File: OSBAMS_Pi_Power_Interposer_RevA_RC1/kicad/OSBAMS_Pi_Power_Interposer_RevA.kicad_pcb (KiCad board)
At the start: 2 copper layers, 57 x 22 mm, 4 parts, among them J1 43045-0400, J2 2x20 stacking socket, K1 KEY M2.5, K2 KEY M2.5

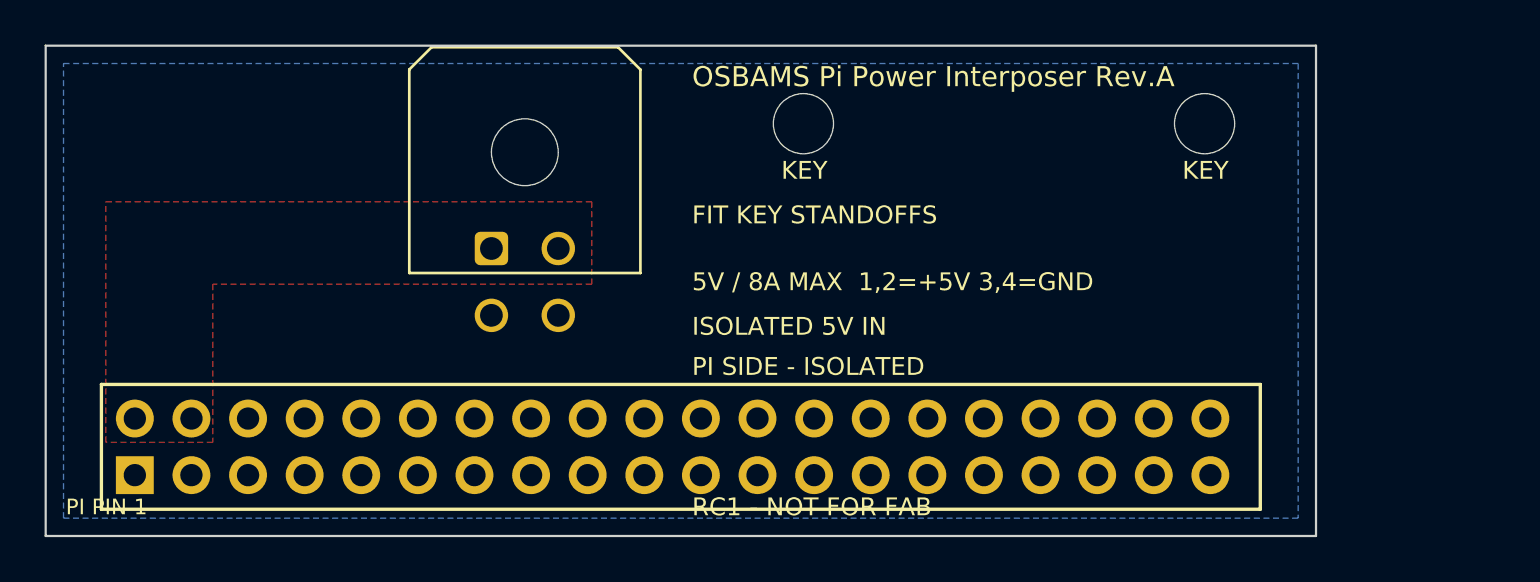
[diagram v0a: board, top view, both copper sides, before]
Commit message: F1 -> Littelfuse 407 8A time-lag (0407008.WR); F2 verified; interposer to HAT+ geometry
Remove 0453008.MRL (very fast-acting). F1 datasheet values and 1206 land pattern
implemented; F2 footprint verified against 451/453 datasheet. Interposer now 65 mm
with M2.5 mounting holes per HAT+ spec. RC2 still gated: socket MPN, Pi 5 STEP
keying check, KiCad 10 ERC.

Co-Authored-By: Claude Sonnet 5.5 <noreply@anthropic.com>
Claude-Session: https://claude.ai/code/session_01ENatZXrEDA18PaxUrZWrpi
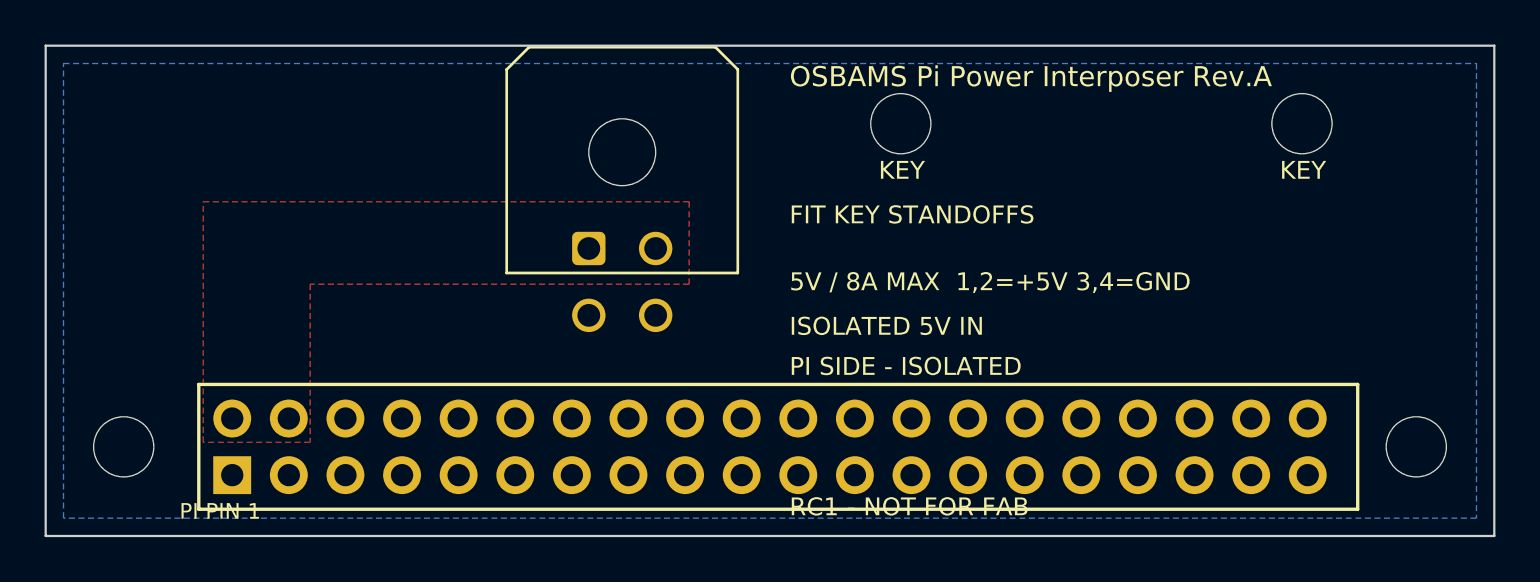
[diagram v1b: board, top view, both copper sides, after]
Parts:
- added M1: M2.5 to Pi, OSBAMS_PiPwr:MountingHole_2.7mm_M2.5, F.Cu at (3.50, 20.0)
- added M2: M2.5 to Pi, OSBAMS_PiPwr:MountingHole_2.7mm_M2.5, F.Cu at (61.5, 20.0)
- moved J1 4.37 mm to (24.4, 11.1)
- moved J2 4.37 mm to (8.37, 20.0)
- moved K1 4.37 mm to (38.4, 5.50)
- moved K2 4.37 mm to (56.4, 5.50)
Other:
- board size 57 x 22 mm -> 65 x 22 mm

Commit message: Pi 5 drawing-based 180-degree key check; move key posts onto bare PCB
Official drawing RP-008347 digitised: reversed posts now land on bare PCB (1.6/3.3 mm clear
of components); correct orientation hangs beyond the Pi edge. Gate: key check passes in plan
view; heights pending SSW-120 drawing.

Co-Authored-By: Claude Sonnet 5.5 <noreply@anthropic.com>
Claude-Session: https://claude.ai/code/session_01ENatZXrEDA18PaxUrZWrpi
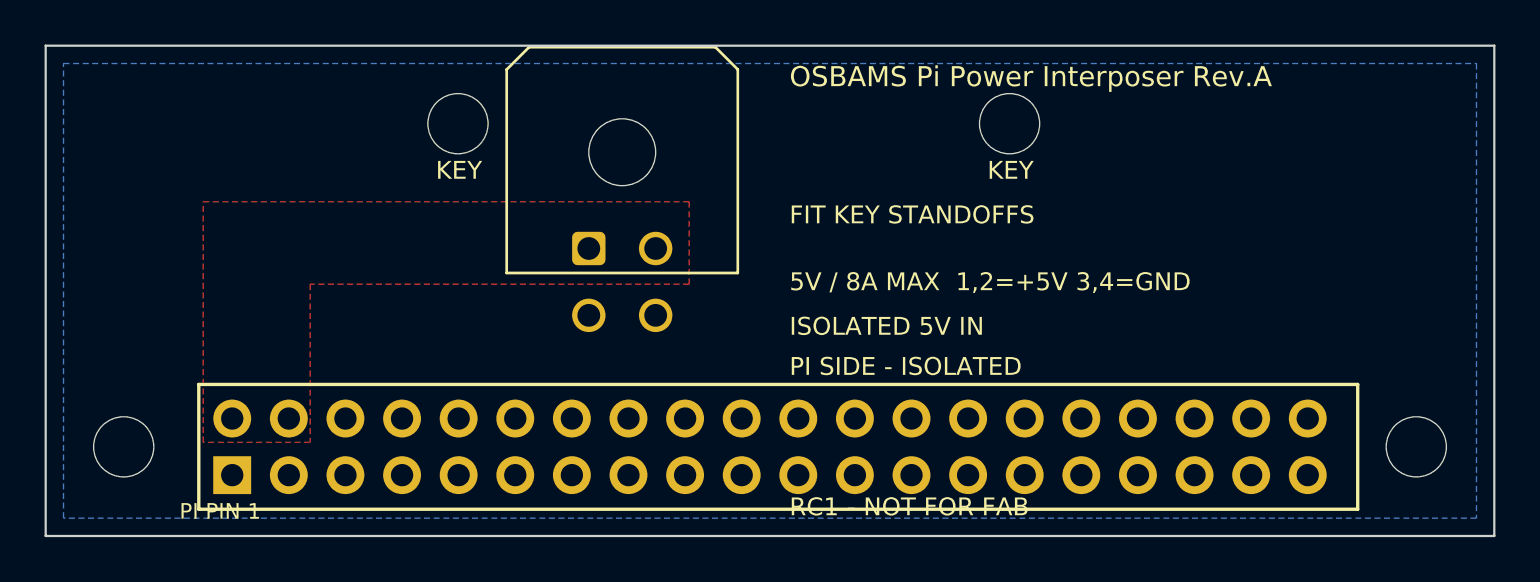
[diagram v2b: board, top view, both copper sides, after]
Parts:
- moved K1 19.9 mm to (18.5, 5.50)
- moved K2 13.1 mm to (43.2, 5.50)
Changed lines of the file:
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@@
   (net 1 "5V_PI")
   (net 2 "PI_GND")
+  (footprint "OSBAMS_PiPwr:KeyStandoff_M2.5" (layer "F.Cu")
+    (at 18.5 5.5)
+    (fp_text reference "K1" (at 0 0) (layer "F.Fab")
+        (effects (font (size 1.27 1.27) (thickness 0.15)))
+    )
+    (fp_text value "KEY M2.5" (at 0 0) (layer "F.SilkS") hide
+        (effects (font (size 1.27 1.27) (thickness 0.15)))
+    )
+    (pad "" np_thru_hole circle (at 0 0) (size 2.7 2.7) (drill 2.7) (layers "F&B.Cu" "*.Mask"))
+  )
+  (footprint "OSBAMS_PiPwr:KeyStandoff_M2.5" (layer "F.Cu")
+    (at 43.25 5.5)
+    (fp_text reference "K2" (at 0 0) (layer "F.Fab")
+        (effects (font (size 1.27 1.27) (thickness 0.15)))
+    )
+    (fp_text value "KEY M2.5" (at 0 0) (layer "F.SilkS") hide
+        (effects (font (size 1.27 1.27) (thickness 0.15)))
+    )
+    (pad "" np_thru_hole circle (at 0 0) (size 2.7 2.7) (drill 2.7) (layers "F&B.Cu" "*.Mask"))
+  )
   (footprint "OSBAMS_PiPwr:MountingHole_2.7mm_M2.5" (layer "F.Cu")
     (at 61.5 20)
     (fp_text reference "M2" (at 0 0) (layer "F.Fab")
-        (effects (font (size 1.27 1.27) (thickness 0.15)))
-    )
-    (fp_text value "M2.5 to Pi" (at 0 0) (layer "F.SilkS") hide
-        (effects (font (size 1.27 1.27) (thickness 0.15)))
-    )
-    (pad "" np_thru_hole circle (at 0 0) (size 2.7 2.7) (drill 2.7) (layers "F&B.Cu" "*.Mask"))
-  )
-  (footprint "OSBAMS_PiPwr:KeyStandoff_M2.5" (layer "F.Cu")
-    (at 38.37 5.5)
-    (fp_text reference "K1" (at 0 0) (layer "F.Fab")
-        (effects (font (size 1.27 1.27) (thickness 0.15)))
-    )
-    (fp_text value "KEY M2.5" (at 0 0) (layer "F.SilkS") hide
-        (effects (font (size 1.27 1.27) (thickness 0.15)))
-    )
-    (pad "" np_thru_hole circle (at 0 0) (size 2.7 2.7) (drill 2.7) (layers "F&B.Cu" "*.Mask"))
-  )
-  (footprint "OSBAMS_PiPwr:KeyStandoff_M2.5" (layer "F.Cu")
-    (at 56.37 5.5)
-    (fp_text reference "K2" (at 0 0) (layer "F.Fab")
-        (effects (font (size 1.27 1.27) (thickness 0.15)))
-    )
-    (fp_text value "KEY M2.5" (at 0 0) (layer "F.SilkS") hide
-        (effects (font (size 1.27 1.27) (thickness 0.15)))
-    )
-    (pad "" np_thru_hole circle (at 0 0) (size 2.7 2.7) (drill 2.7) (layers "F&B.Cu" "*.Mask"))
-  )
-  (footprint "OSBAMS_PiPwr:MountingHole_2.7mm_M2.5" (layer "F.Cu")
-    (at 3.5 20)
-    (fp_text reference "M1" (at 0 0) (layer "F.Fab")
         (effects (font (size 1.27 1.27) (thickness 0.15)))
     )
@@
     )
   )
+  (footprint "OSBAMS_PiPwr:MountingHole_2.7mm_M2.5" (layer "F.Cu")
+    (at 3.5 20)
+    (fp_text reference "M1" (at 0 0) (layer "F.Fab")
+        (effects (font (size 1.27 1.27) (thickness 0.15)))
+    )
+    (fp_text value "M2.5 to Pi" (at 0 0) (layer "F.SilkS") hide
+        (effects (font (size 1.27 1.27) (thickness 0.15)))
+    )
+    (pad "" np_thru_hole circle (at 0 0) (size 2.7 2.7) (drill 2.7) (layers "F&B.Cu" "*.Mask"))
+  )
   (gr_line (start 65 2) (end 65 24)
     (stroke (width 0.1) (type default)) (layer "Edge.Cuts"))
+  (gr_line (start 0 24) (end 0 2)
+    (stroke (width 0.1) (type default)) (layer "Edge.Cuts"))
   (gr_line (start 0 2) (end 65 2)
     (stroke (width 0.1) (type default)) (layer "Edge.Cuts"))
-  (gr_line (start 0 24) (end 0 2)
-    (stroke (width 0.1) (type default)) (layer "Edge.Cuts"))
   (gr_line (start 65 24) (end 0 24)
     (stroke (width 0.1) (type default)) (layer "Edge.Cuts"))
@@
     (effects (font (size 0.8 0.8) (thickness 0.18)) (justify left))
   )
-  (gr_text "FIT KEY STANDOFFS" (at 33.37 9.6) (layer "F.SilkS")
-    (effects (font (size 0.8 0.8) (thickness 0.18)) (justify left))
-  )
-  (gr_text "KEY" (at 55.37 7.6) (layer "F.SilkS")
+  (gr_text "RC1 - NOT FOR FAB" (at 33.37 22.7) (layer "F.SilkS")
+    (effects (font (size 0.8 0.8) (thickness 0.18)) (justify left))
+  )
+  (gr_text "OSBAMS Pi Power Interposer Rev.A" (at 33.37 3.4) (layer "F.SilkS")
+    (effects (font (size 0.9 0.9) (thickness 0.18)) (justify left))
+  )
+  (gr_text "5V / 8A MAX  1,2=+5V 3,4=GND" (at 33.37 12.6) (layer "F.SilkS")
     (effects (font (size 0.8 0.8) (thickness 0.18)) (justify left))
   )
@@
     (effects (font (size 0.7 0.7) (thickness 0.18)) (justify left))
   )
+  (gr_text "PI SIDE - ISOLATED" (at 33.37 16.399999) (layer "F.SilkS")
+    (effects (font (size 0.8 0.8) (thickness 0.18)) (justify left))
+  )
+  (gr_text "KEY" (at 42.25 7.6) (layer "F.SilkS")
+    (effects (font (size 0.8 0.8) (thickness 0.18)) (justify left))
+  )
+  (gr_text "KEY" (at 17.5 7.6) (layer "F.SilkS")
+    (effects (font (size 0.8 0.8) (thickness 0.18)) (justify left))
+  )
+  (gr_text "FIT KEY STANDOFFS" (at 33.37 9.6) (layer "F.SilkS")
+    (effects (font (size 0.8 0.8) (thickness 0.18)) (justify left))
+  )
   (gr_text "ISOLATED 5V IN" (at 33.37 14.6) (layer "F.SilkS")
     (effects (font (size 0.8 0.8) (thickness 0.18)) (justify left))
   )
-  (gr_text "OSBAMS Pi Power Interposer Rev.A" (at 33.37 3.4) (layer "F.SilkS")
-    (effects (font (size 0.9 0.9) (thickness 0.18)) (justify left))
-  )
-  (gr_text "PI SIDE - ISOLATED" (at 33.37 16.399999) (layer "F.SilkS")
-    (effects (font (size 0.8 0.8) (thickness 0.18)) (justify left))
-  )
-  (gr_text "5V / 8A MAX  1,2=+5V 3,4=GND" (at 33.37 12.6) (layer "F.SilkS")
-    (effects (font (size 0.8 0.8) (thickness 0.18)) (justify left))
-  )
-  (gr_text "KEY" (at 37.37 7.6) (layer "F.SilkS")
-    (effects (font (size 0.8 0.8) (thickness 0.18)) (justify left))
-  )
-  (gr_text "RC1 - NOT FOR FAB" (at 33.37 22.7) (layer "F.SilkS")
-    (effects (font (size 0.8 0.8) (thickness 0.18)) (justify left))
-  )

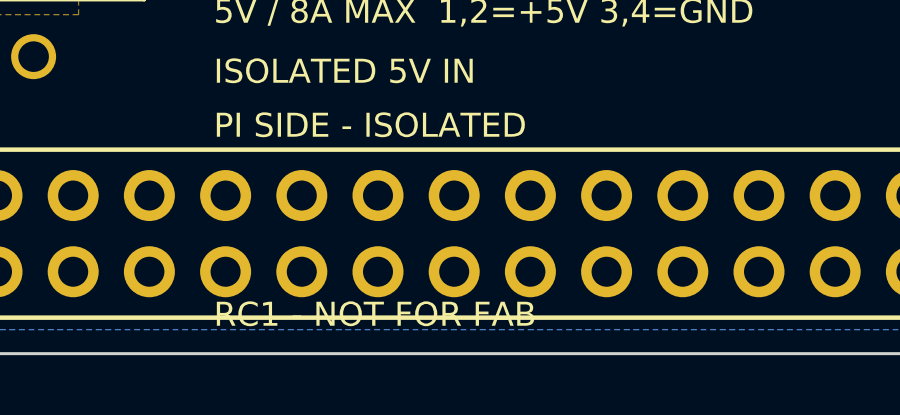
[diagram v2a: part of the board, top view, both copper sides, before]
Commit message: Interposer around Samtec SSW-120-01-S-D; stack-height check; make_rc2 gate tool
Body 8.51 mm -> 11 mm M2.5 spacers, 20 mm key posts (+2.5 mm margin over pin tips). Socket
contact resistance stays a conservative first-article-measured placeholder. RC2 gate: only
KiCad 10 ERC remains; make_rc2.sh refuses until then.

Co-Authored-By: Claude Sonnet 5.5 <noreply@anthropic.com>
Claude-Session: https://claude.ai/code/session_01ENatZXrEDA18PaxUrZWrpi
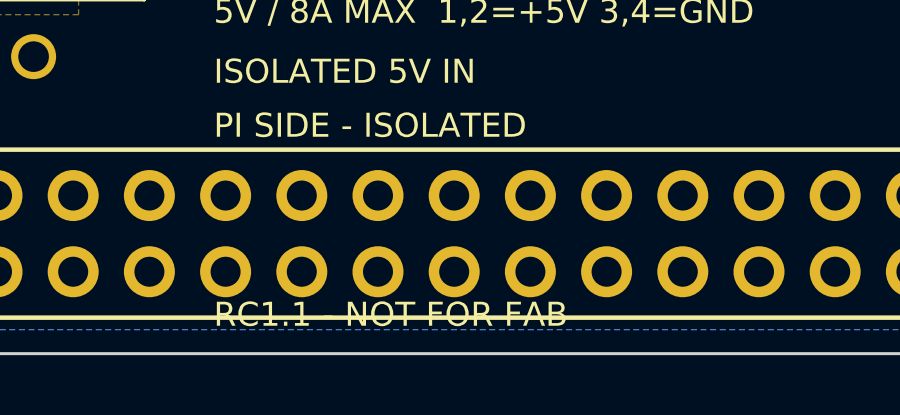
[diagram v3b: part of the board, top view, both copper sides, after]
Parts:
- J2: value 2x20 stacking socket -> SSW-120-01-S-D; footprint OSBAMS_PiPwr:PinSocket_2x20_P2.54mm_RPi_TopView -> OSBAMS_PiPwr:SSW-120-01-S-D_RPi_TopView
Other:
- board text added: "RC1.1 - NOT FOR FAB"
- board text removed: "RC1 - NOT FOR FAB"
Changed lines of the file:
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@@
   (net 1 "5V_PI")
   (net 2 "PI_GND")
-  (footprint "OSBAMS_PiPwr:KeyStandoff_M2.5" (layer "F.Cu")
-    (at 18.5 5.5)
-    (fp_text reference "K1" (at 0 0) (layer "F.Fab")
-        (effects (font (size 1.27 1.27) (thickness 0.15)))
-    )
-    (fp_text value "KEY M2.5" (at 0 0) (layer "F.SilkS") hide
-        (effects (font (size 1.27 1.27) (thickness 0.15)))
-    )
-    (pad "" np_thru_hole circle (at 0 0) (size 2.7 2.7) (drill 2.7) (layers "F&B.Cu" "*.Mask"))
-  )
-  (footprint "OSBAMS_PiPwr:KeyStandoff_M2.5" (layer "F.Cu")
-    (at 43.25 5.5)
-    (fp_text reference "K2" (at 0 0) (layer "F.Fab")
-        (effects (font (size 1.27 1.27) (thickness 0.15)))
-    )
-    (fp_text value "KEY M2.5" (at 0 0) (layer "F.SilkS") hide
-        (effects (font (size 1.27 1.27) (thickness 0.15)))
-    )
-    (pad "" np_thru_hole circle (at 0 0) (size 2.7 2.7) (drill 2.7) (layers "F&B.Cu" "*.Mask"))
-  )
-  (footprint "OSBAMS_PiPwr:MountingHole_2.7mm_M2.5" (layer "F.Cu")
-    (at 61.5 20)
-    (fp_text reference "M2" (at 0 0) (layer "F.Fab")
-        (effects (font (size 1.27 1.27) (thickness 0.15)))
-    )
-    (fp_text value "M2.5 to Pi" (at 0 0) (layer "F.SilkS") hide
-        (effects (font (size 1.27 1.27) (thickness 0.15)))
-    )
-    (pad "" np_thru_hole circle (at 0 0) (size 2.7 2.7) (drill 2.7) (layers "F&B.Cu" "*.Mask"))
-  )
-  (footprint "OSBAMS_PiPwr:PinSocket_2x20_P2.54mm_RPi_TopView" (layer "F.Cu")
+  (footprint "OSBAMS_PiPwr:SSW-120-01-S-D_RPi_TopView" (layer "F.Cu")
     (at 8.37 20)
     (fp_text reference "J2" (at 0 0) (layer "F.Fab")
         (effects (font (size 1.27 1.27) (thickness 0.15)))
     )
-    (fp_text value "2x20 stacking socket" (at 0 0) (layer "F.SilkS") hide
+    (fp_text value "SSW-120-01-S-D" (at 0 0) (layer "F.SilkS") hide
         (effects (font (size 1.27 1.27) (thickness 0.15)))
     )
@@
     (pad "40" thru_hole circle (at 48.259999 -1.269999) (size 1.7 1.7) (drill 1) (layers "*.Cu" "*.Mask"))
   )
+  (footprint "OSBAMS_PiPwr:MountingHole_2.7mm_M2.5" (layer "F.Cu")
+    (at 3.5 20)
+    (fp_text reference "M1" (at 0 0) (layer "F.Fab")
+        (effects (font (size 1.27 1.27) (thickness 0.15)))
+    )
+    (fp_text value "M2.5 to Pi" (at 0 0) (layer "F.SilkS") hide
+        (effects (font (size 1.27 1.27) (thickness 0.15)))
+    )
+    (pad "" np_thru_hole circle (at 0 0) (size 2.7 2.7) (drill 2.7) (layers "F&B.Cu" "*.Mask"))
+  )
+  (footprint "OSBAMS_PiPwr:KeyStandoff_M2.5" (layer "F.Cu")
+    (at 18.5 5.5)
+    (fp_text reference "K1" (at 0 0) (layer "F.Fab")
+        (effects (font (size 1.27 1.27) (thickness 0.15)))
+    )
+    (fp_text value "KEY M2.5" (at 0 0) (layer "F.SilkS") hide
+        (effects (font (size 1.27 1.27) (thickness 0.15)))
+    )
+    (pad "" np_thru_hole circle (at 0 0) (size 2.7 2.7) (drill 2.7) (layers "F&B.Cu" "*.Mask"))
+  )
+  (footprint "OSBAMS_PiPwr:KeyStandoff_M2.5" (layer "F.Cu")
+    (at 43.25 5.5)
+    (fp_text reference "K2" (at 0 0) (layer "F.Fab")
+        (effects (font (size 1.27 1.27) (thickness 0.15)))
+    )
+    (fp_text value "KEY M2.5" (at 0 0) (layer "F.SilkS") hide
+        (effects (font (size 1.27 1.27) (thickness 0.15)))
+    )
+    (pad "" np_thru_hole circle (at 0 0) (size 2.7 2.7) (drill 2.7) (layers "F&B.Cu" "*.Mask"))
+  )
   (footprint "Connector_Molex:Molex_Micro-Fit_3.0_43045-0400_2x02_P3.00mm_Horizontal" (layer "F.Cu")
     (at 24.37 11.1)
@@
   )
   (footprint "OSBAMS_PiPwr:MountingHole_2.7mm_M2.5" (layer "F.Cu")
-    (at 3.5 20)
-    (fp_text reference "M1" (at 0 0) (layer "F.Fab")
+    (at 61.5 20)
+    (fp_text reference "M2" (at 0 0) (layer "F.Fab")
         (effects (font (size 1.27 1.27) (thickness 0.15)))
     )
@@
     (pad "" np_thru_hole circle (at 0 0) (size 2.7 2.7) (drill 2.7) (layers "F&B.Cu" "*.Mask"))
   )
+  (gr_line (start 65 24) (end 0 24)
+    (stroke (width 0.1) (type default)) (layer "Edge.Cuts"))
   (gr_line (start 65 2) (end 65 24)
     (stroke (width 0.1) (type default)) (layer "Edge.Cuts"))
@@
   (gr_line (start 0 2) (end 65 2)
     (stroke (width 0.1) (type default)) (layer "Edge.Cuts"))
-  (gr_line (start 65 24) (end 0 24)
-    (stroke (width 0.1) (type default)) (layer "Edge.Cuts"))
   (gr_text "Rev.A  2oz Cu  1.6mm" (at 34.37 21.2) (layer "B.SilkS")
-    (effects (font (size 0.8 0.8) (thickness 0.18)) (justify left))
-  )
-  (gr_text "RC1 - NOT FOR FAB" (at 33.37 22.7) (layer "F.SilkS")
     (effects (font (size 0.8 0.8) (thickness 0.18)) (justify left))
   )
@@
     (effects (font (size 0.9 0.9) (thickness 0.18)) (justify left))
   )
-  (gr_text "5V / 8A MAX  1,2=+5V 3,4=GND" (at 33.37 12.6) (layer "F.SilkS")
+  (gr_text "PI SIDE - ISOLATED" (at 33.37 16.399999) (layer "F.SilkS")
+    (effects (font (size 0.8 0.8) (thickness 0.18)) (justify left))
+  )
+  (gr_text "KEY" (at 42.25 7.6) (layer "F.SilkS")
+    (effects (font (size 0.8 0.8) (thickness 0.18)) (justify left))
+  )
+  (gr_text "FIT KEY STANDOFFS" (at 33.37 9.6) (layer "F.SilkS")
+    (effects (font (size 0.8 0.8) (thickness 0.18)) (justify left))
+  )
+  (gr_text "KEY" (at 17.5 7.6) (layer "F.SilkS")
+    (effects (font (size 0.8 0.8) (thickness 0.18)) (justify left))
+  )
+  (gr_text "RC1.1 - NOT FOR FAB" (at 33.37 22.7) (layer "F.SilkS")
     (effects (font (size 0.8 0.8) (thickness 0.18)) (justify left))
   )
@@
     (effects (font (size 0.7 0.7) (thickness 0.18)) (justify left))
   )
-  (gr_text "PI SIDE - ISOLATED" (at 33.37 16.399999) (layer "F.SilkS")
-    (effects (font (size 0.8 0.8) (thickness 0.18)) (justify left))
-  )
-  (gr_text "KEY" (at 42.25 7.6) (layer "F.SilkS")
-    (effects (font (size 0.8 0.8) (thickness 0.18)) (justify left))
-  )
-  (gr_text "KEY" (at 17.5 7.6) (layer "F.SilkS")
-    (effects (font (size 0.8 0.8) (thickness 0.18)) (justify left))
-  )
-  (gr_text "FIT KEY STANDOFFS" (at 33.37 9.6) (layer "F.SilkS")
-    (effects (font (size 0.8 0.8) (thickness 0.18)) (justify left))
-  )
+  (gr_text "5V / 8A MAX  1,2=+5V 3,4=GND" (at 33.37 12.6) (layer "F.SilkS")
+    (effects (font (size 0.8 0.8) (thickness 0.18)) (justify left))
+  )
